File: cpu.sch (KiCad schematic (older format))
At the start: 9 parts, among them IC1 STM32L051K8T6, SW1 SW_PUSH

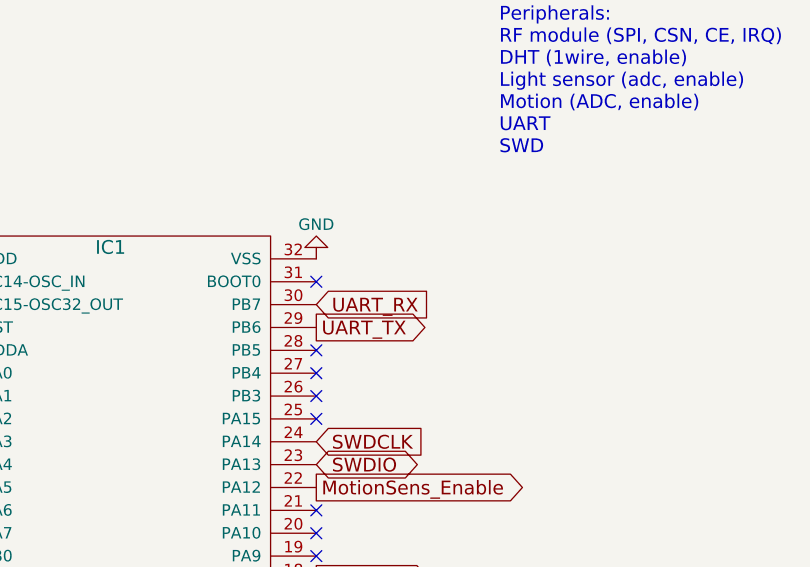
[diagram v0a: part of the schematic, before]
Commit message: Fix Boot0 pin and add prices per component
Signed-off-by: Philip Luyckx <philip.luyckx@gmail.com>
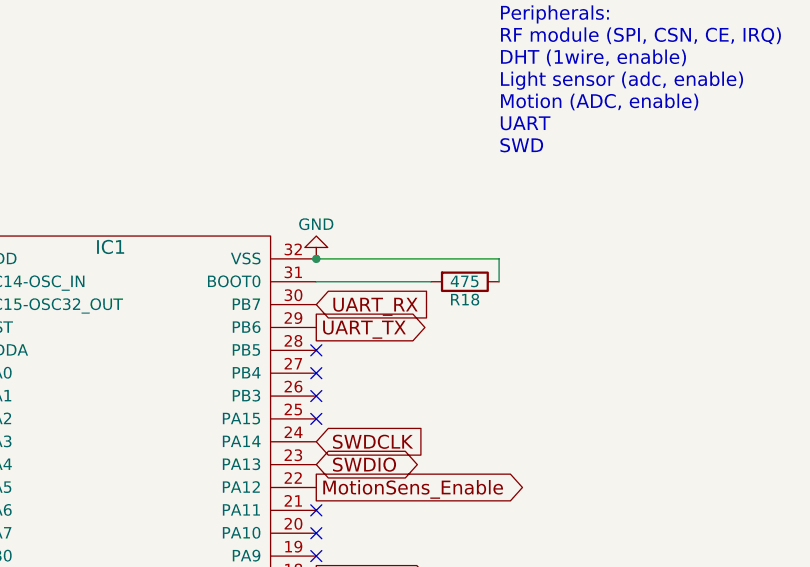
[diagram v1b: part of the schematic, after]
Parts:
- added R18: 475, Resistors_SMD:R_0603, symbol R
- C1, C2, C3, C4, C5, C6: Price (none) -> 0.02
- IC1: Price (none) -> 3.04
- R1: Price (none) -> 0.01
- SW1: Price (none) -> 0.05
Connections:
- net GND: now also R18.1
- net at IC1.31 (BOOT0): now also R18.2
- no-connect marks 8 -> 7
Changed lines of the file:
@@
 F 2 "Resistors_SMD:R_0805" H 2738 3050 30  0001 C CNN
 F 3 "" H 2700 3200 60  0000 C CNN
+F 4 "0.02" H 2700 3200 60  0001 C CNN "Price"
 	1    2700 3200
 	1    0    0    -1
@@
 F 2 "Resistors_SMD:R_0805" H 2988 3050 30  0001 C CNN
 F 3 "" H 2950 3200 60  0000 C CNN
+F 4 "0.02" H 2950 3200 60  0001 C CNN "Price"
 	1    2950 3200
 	1    0    0    -1
@@
 F 2 "Resistors_SMD:R_0805" H 3238 3050 30  0001 C CNN
 F 3 "" H 3200 3200 60  0000 C CNN
+F 4 "0.02" H 3200 3200 60  0001 C CNN "Price"
 	1    3200 3200
 	1    0    0    -1
 $EndComp
-Wire Wire Line
-	2700 3050 3200 3050
-Connection ~ 2950 3050
-Wire Wire Line
-	2700 3350 3200 3350
-Connection ~ 2950 3350
 $Comp
 L VCC #PWR03
@@
 $Comp
 L GND #PWR05
-U 1 1 565E10BA
-P 7050 3100
-F 0 "#PWR05" H 7050 2850 50  0001 C CNN
-F 1 "GND" H 7050 2950 50  0000 C CNN
-F 2 "" H 7050 3100 60  0000 C CNN
-F 3 "" H 7050 3100 60  0000 C CNN
-	1    7050 3100
-	-1   0    0    1
-$EndComp
-$Comp
-L GND #PWR06
 U 1 1 565E10D6
 P 5350 4600
-F 0 "#PWR06" H 5350 4350 50  0001 C CNN
+F 0 "#PWR05" H 5350 4350 50  0001 C CNN
 F 1 "GND" H 5350 4450 50  0000 C CNN
 F 2 "" H 5350 4600 60  0000 C CNN
@@
 F 2 "Resistors_SMD:R_0805" H 2738 4000 30  0001 C CNN
 F 3 "" H 2700 4150 60  0000 C CNN
+F 4 "0.02" H 2700 4150 60  0001 C CNN "Price"
 	1    2700 4150
 	1    0    0    -1
@@
 F 2 "Resistors_SMD:R_0805" H 2988 4000 30  0001 C CNN
 F 3 "" H 2950 4150 60  0000 C CNN
+F 4 "0.02" H 2950 4150 60  0001 C CNN "Price"
 	1    2950 4150
 	1    0    0    -1
 $EndComp
 $Comp
-L VCC #PWR07
+L VCC #PWR06
 U 1 1 565E12D0
 P 2700 4000
-F 0 "#PWR07" H 2700 3850 50  0001 C CNN
+F 0 "#PWR06" H 2700 3850 50  0001 C CNN
 F 1 "VCC" H 2700 4150 50  0000 C CNN
 F 2 "" H 2700 4000 60  0000 C CNN
@@
 $EndComp
 $Comp
-L GND #PWR08
+L GND #PWR07
 U 1 1 565E12F0
 P 2700 4300
-F 0 "#PWR08" H 2700 4050 50  0001 C CNN
+F 0 "#PWR07" H 2700 4050 50  0001 C CNN
 F 1 "GND" H 2700 4150 50  0000 C CNN
 F 2 "" H 2700 4300 60  0000 C CNN
@@
 	1    0    0    -1
 $EndComp
-Wire Wire Line
-	2700 4300 2950 4300
-Wire Wire Line
-	2700 4000 2950 4000
-Wire Notes Line
-	2550 2800 3500 2800
-Wire Notes Line
-	3500 2800 3500 3550
-Wire Notes Line
-	3500 3550 2550 3550
-Wire Notes Line
-	2550 3550 2550 2800
-Wire Notes Line
-	2550 3750 3500 3750
-Wire Notes Line
-	3500 3750 3500 4500
-Wire Notes Line
-	3500 4500 2550 4500
-Wire Notes Line
-	2550 4500 2550 3750
 Text Notes 2550 3750 0    60   ~ 0
 Close to VDDA
@@
 F 2 "Resistors_SMD:R_0805" H 2988 5400 30  0001 C CNN
 F 3 "" H 2950 5550 60  0000 C CNN
+F 4 "0.02" H 2950 5550 60  0001 C CNN "Price"
 	1    2950 5550
 	1    0    0    -1
@@
 F 2 "CustomSmd:MicroSwitch_6x6mm" H 2700 5700 60  0001 C CNN
 F 3 "" H 2700 5700 60  0000 C CNN
+F 4 "0.05" H 2700 5700 60  0001 C CNN "Price"
 	1    2700 5700
 	0    1    1    0
@@
 F 2 "Resistors_SMD:R_0603" V 2880 5100 30  0001 C CNN
 F 3 "" H 2950 5100 30  0000 C CNN
+F 4 "0.01" V 2950 5100 60  0001 C CNN "Price"
 	1    2950 5100
 	1    0    0    -1
 $EndComp
 $Comp
-L VCC #PWR09
+L VCC #PWR08
 U 1 1 565E15CE
 P 2950 4950
-F 0 "#PWR09" H 2950 4800 50  0001 C CNN
+F 0 "#PWR08" H 2950 4800 50  0001 C CNN
 F 1 "VCC" H 2950 5100 50  0000 C CNN
 F 2 "" H 2950 4950 60  0000 C CNN
@@
 $EndComp
 $Comp
-L GND #PWR010
+L GND #PWR09
 U 1 1 565E15F4
 P 2950 6000
-F 0 "#PWR010" H 2950 5750 50  0001 C CNN
+F 0 "#PWR09" H 2950 5750 50  0001 C CNN
 F 1 "GND" H 2950 5850 50  0000 C CNN
 F 2 "" H 2950 6000 60  0000 C CNN
@@
 	1    0    0    -1
 $EndComp
-Wire Wire Line
-	2700 6000 2950 6000
-Wire Wire Line
-	2950 6000 2950 5700
-Wire Wire Line
-	2700 5400 2950 5400
-Wire Wire Line
-	2950 5400 2950 5250
-Wire Wire Line
-	2950 5300 3250 5300
-Connection ~ 2950 5300
 Text GLabel 3250 5300 2    60   Output ~ 0
 MCU_RST
@@
 MCU_RST
 $Comp
-L VCC #PWR011
+L VCC #PWR010
 U 1 1 565E178E
 P 4300 3500
-F 0 "#PWR011" H 4300 3350 50  0001 C CNN
+F 0 "#PWR010" H 4300 3350 50  0001 C CNN
 F 1 "VCC" H 4300 3650 50  0000 C CNN
 F 2 "" H 4300 3500 60  0000 C CNN
@@
 	1    0    0    -1
 $EndComp
-Wire Wire Line
-	4300 3500 5350 3500
-Wire Notes Line
-	2550 4700 3200 4700
-Wire Notes Line
-	3200 4700 3200 6200
-Wire Notes Line
-	3200 6200 2550 6200
-Wire Notes Line
-	2550 6200 2550 4700
 Text Notes 2550 4700 0    60   ~ 0
 Reset circuit
@@
 Text GLabel 5350 4400 0    60   Input ~ 0
 RF_IRQ
-NoConn ~ 7050 3200
 Text Notes 7850 2650 0    60   ~ 0
 Peripherals:\nRF module (SPI, CSN, CE, IRQ)\nDHT (1wire, enable)\nLight sensor (adc, enable)\nMotion (ADC, enable)\nUART\nSWD
@@
 F 2 "STM32:STM32L051-LQFP32" H 5550 3000 60  0001 C CNN
 F 3 "" H 5550 3000 60  0000 C CNN
+F 4 "3.04" H 6200 3000 60  0001 C CNN "Price"
 	1    6200 3000
 	1    0    0    -1
@@
 Text GLabel 7050 4500 2    60   Output ~ 0
 Enable5V
+$Comp
+L GND #PWR011
+U 1 1 565E10BA
+P 7050 3100
+F 0 "#PWR011" H 7050 2850 50  0001 C CNN
+F 1 "GND" H 7050 2950 50  0000 C CNN
+F 2 "" H 7050 3100 60  0000 C CNN
+F 3 "" H 7050 3100 60  0000 C CNN
+	1    7050 3100
+	-1   0    0    1
+$EndComp
+Wire Wire Line
+	2700 3050 3200 3050
+Connection ~ 2950 3050
+Wire Wire Line
+	2700 3350 3200 3350
+Connection ~ 2950 3350
+Wire Wire Line
+	2700 4300 2950 4300
+Wire Wire Line
+	2700 4000 2950 4000
+Wire Notes Line
+	2550 2800 3500 2800
+Wire Notes Line
+	3500 2800 3500 3550
+Wire Notes Line
+	3500 3550 2550 3550
+Wire Notes Line
+	2550 3550 2550 2800
+Wire Notes Line
+	2550 3750 3500 3750
+Wire Notes Line
+	3500 3750 3500 4500
+Wire Notes Line
+	3500 4500 2550 4500
+Wire Notes Line
+	2550 4500 2550 3750
+Wire Wire Line
+	2700 6000 2950 6000
+Wire Wire Line
+	2950 6000 2950 5700
+Wire Wire Line
+	2700 5400 2950 5400
+Wire Wire Line
+	2950 5400 2950 5250
+Wire Wire Line
+	2950 5300 3250 5300
+Connection ~ 2950 5300
+Wire Wire Line
+	4300 3500 5350 3500
+Wire Notes Line
+	2550 4700 3200 4700
+Wire Notes Line
+	3200 4700 3200 6200
+Wire Notes Line
+	3200 6200 2550 6200
+Wire Notes Line
+	2550 6200 2550 4700
+Connection ~ 7050 3100
+Wire Wire Line
+	7050 3200 7550 3200
+Wire Wire Line
+	7850 3100 7050 3100
+Wire Wire Line
+	7850 3200 7850 3100
+$Comp
+L R R18
+U 1 1 56EEC619
+P 7700 3200
+F 0 "R18" V 7780 3200 50  0000 C CNN
+F 1 "475" V 7700 3200 50  0000 C CNN
+F 2 "Resistors_SMD:R_0603" V 7630 3200 50  0001 C CNN
+F 3 "" H 7700 3200 50  0000 C CNN
+F 4 "0.01" V 7700 3200 60  0001 C CNN "Price"
+	1    7700 3200
+	0    1    1    0
+$EndComp
 $EndSCHEMATC

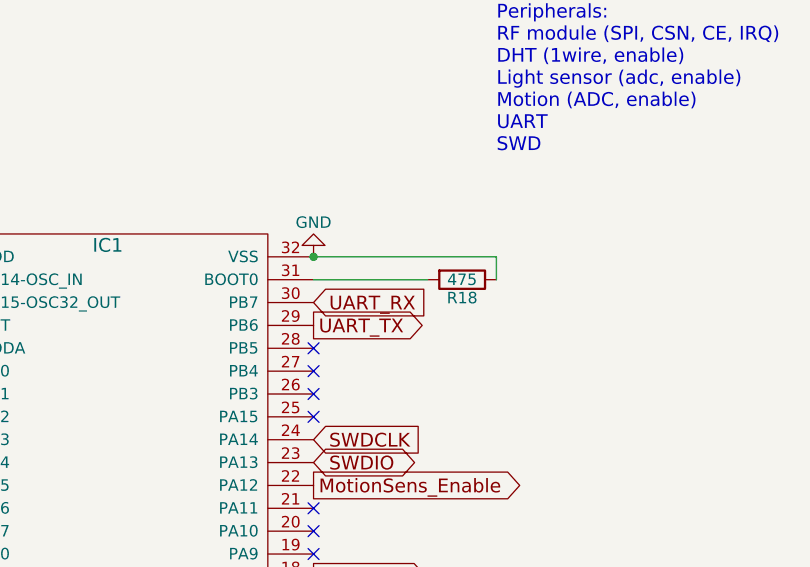
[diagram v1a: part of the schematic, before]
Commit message: Fix Boot0 pin and mechanical problem with the Fresnel lens
 * Resistor at Boot0 pin not necessary:
     it is only input and can directly connected to ground
 * The capacitors above the cpu on the bottom layer are not
     correctly placed: there is a problem when placing the
     Fresnel lens.

Signed-off-by: Philip Luyckx <philip.luyckx@gmail.com>
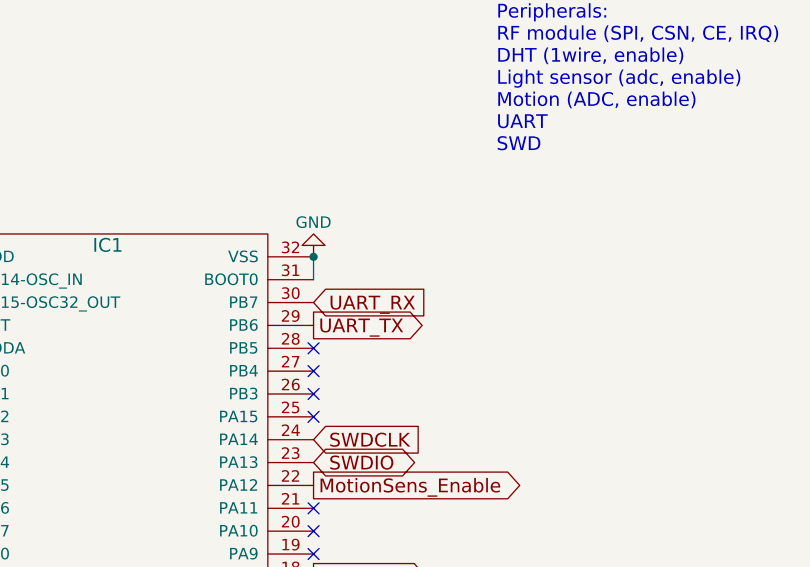
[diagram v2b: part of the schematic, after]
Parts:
- removed R18: 475, Resistors_SMD:R_0603, symbol R
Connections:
- net GND: now also IC1.31 (BOOT0)
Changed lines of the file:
@@
 Connection ~ 7050 3100
 Wire Wire Line
-	7050 3200 7550 3200
-Wire Wire Line
-	7850 3100 7050 3100
-Wire Wire Line
-	7850 3200 7850 3100
-$Comp
-L R R18
-U 1 1 56EEC619
-P 7700 3200
-F 0 "R18" V 7780 3200 50  0000 C CNN
-F 1 "475" V 7700 3200 50  0000 C CNN
-F 2 "Resistors_SMD:R_0603" V 7630 3200 50  0001 C CNN
-F 3 "" H 7700 3200 50  0000 C CNN
-F 4 "0.01" V 7700 3200 60  0001 C CNN "Price"
-	1    7700 3200
-	0    1    1    0
-$EndComp
+	7050 3100 7050 3200
 $EndSCHEMATC
